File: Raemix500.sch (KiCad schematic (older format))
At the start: 0 parts

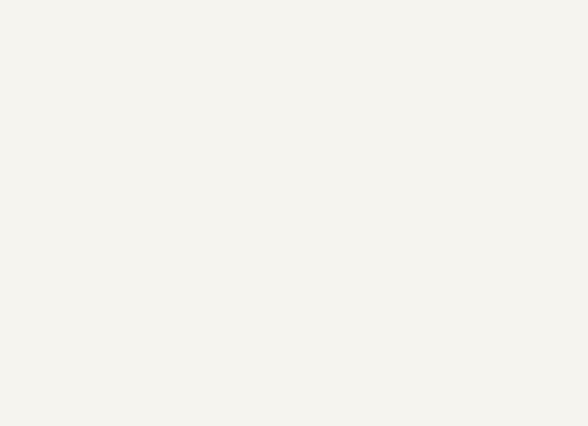
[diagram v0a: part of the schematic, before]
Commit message: Add expansion bus
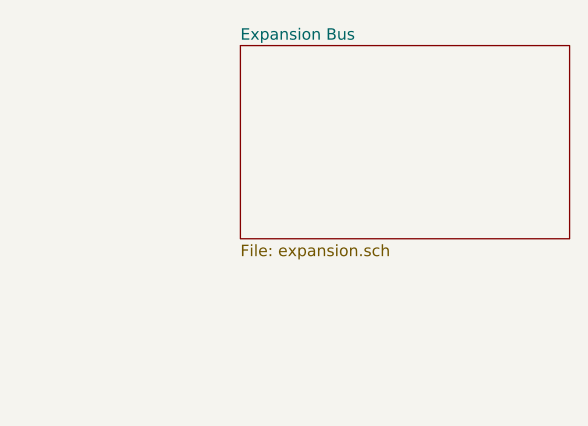
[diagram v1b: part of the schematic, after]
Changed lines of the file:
@@
 $Descr A4 11693 8268
 encoding utf-8
-Sheet 1 10
+Sheet 1 11
 Title "Rämixx500"
 Date "2019-04-17"
@@
 F1 "clockdist.sch" 50
 $EndSheet
+$Sheet
+S 9455 1420 1440 845
+U 5E813DC5
+F0 "Expansion Bus" 50
+F1 "expansion.sch" 50
+$EndSheet
 $EndSCHEMATC

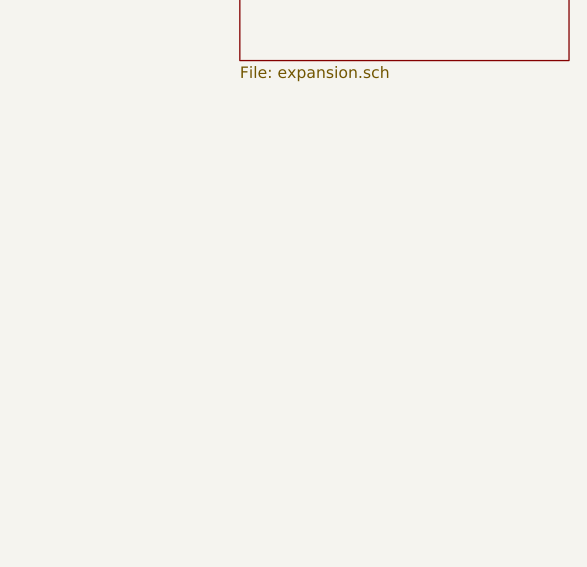
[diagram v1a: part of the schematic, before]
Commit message: Add power & decoupling, not yet complete
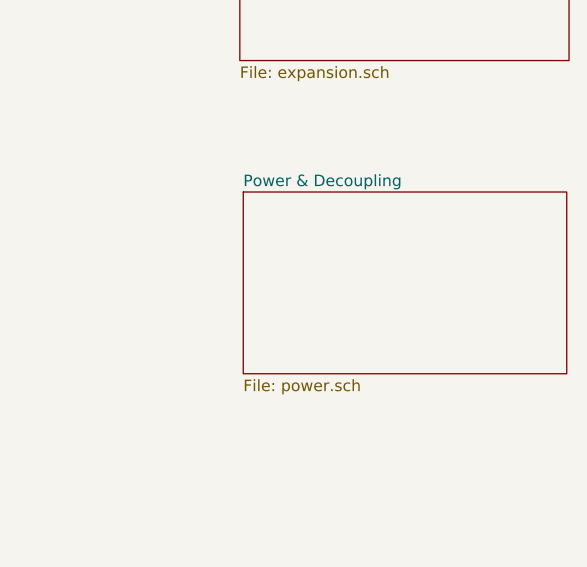
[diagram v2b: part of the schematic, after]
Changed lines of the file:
@@
 $Descr A4 11693 8268
 encoding utf-8
-Sheet 1 11
+Sheet 1 12
 Title "Rämixx500"
 Date "2019-04-17"
@@
 F1 "expansion.sch" 50
 $EndSheet
+$Sheet
+S 9470 2840 1415 795
+U 5E9E4C57
+F0 "Power & Decoupling" 50
+F1 "power.sch" 50
+$EndSheet
 $EndSCHEMATC

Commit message: Add RTC
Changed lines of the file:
@@
 $Descr A4 11693 8268
 encoding utf-8
-Sheet 1 12
+Sheet 1 13
 Title "Rämixx500"
 Date "2019-04-17"
@@
 F1 "power.sch" 50
 $EndSheet
+$Sheet
+S 4060 4220 1380 860
+U 5CF615AB
+F0 "Real-Time Clock" 50
+F1 "rtc.sch" 50
+$EndSheet
 $EndSCHEMATC

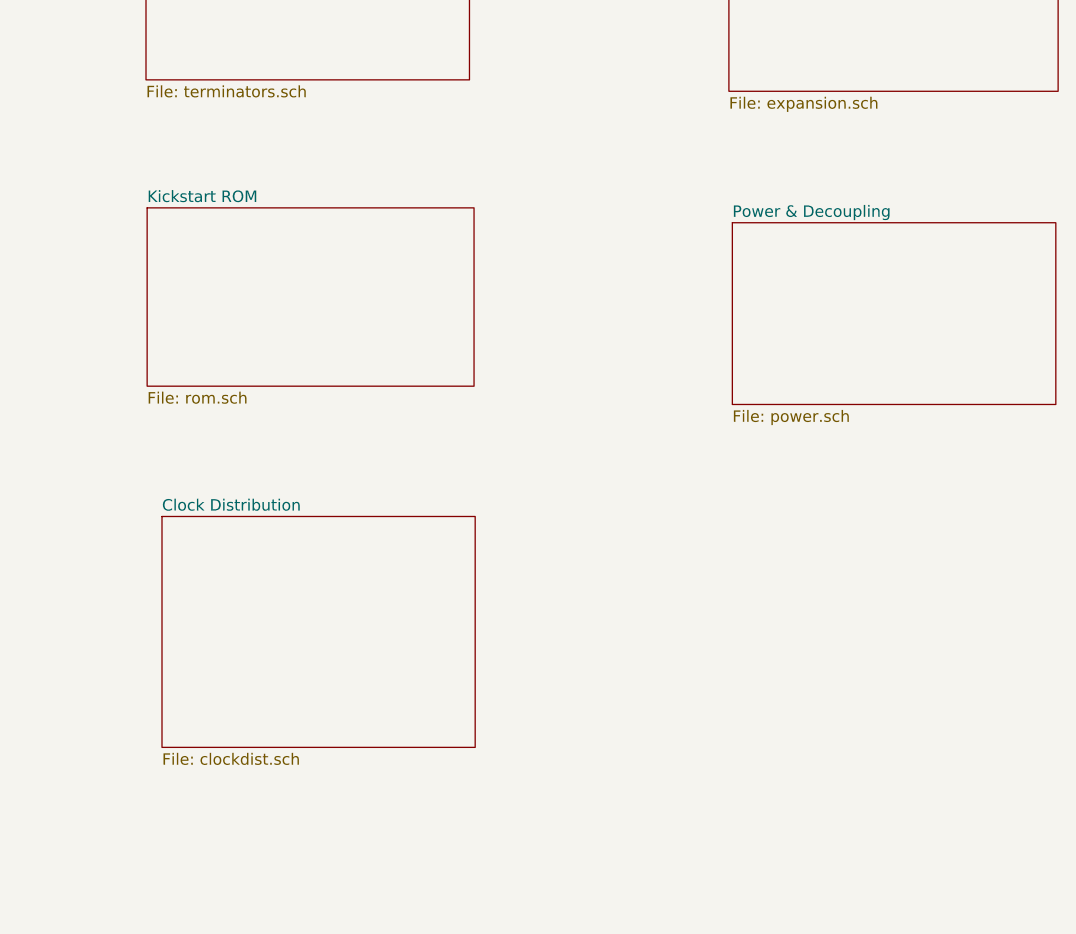
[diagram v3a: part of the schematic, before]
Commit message: Add trapdoor connector
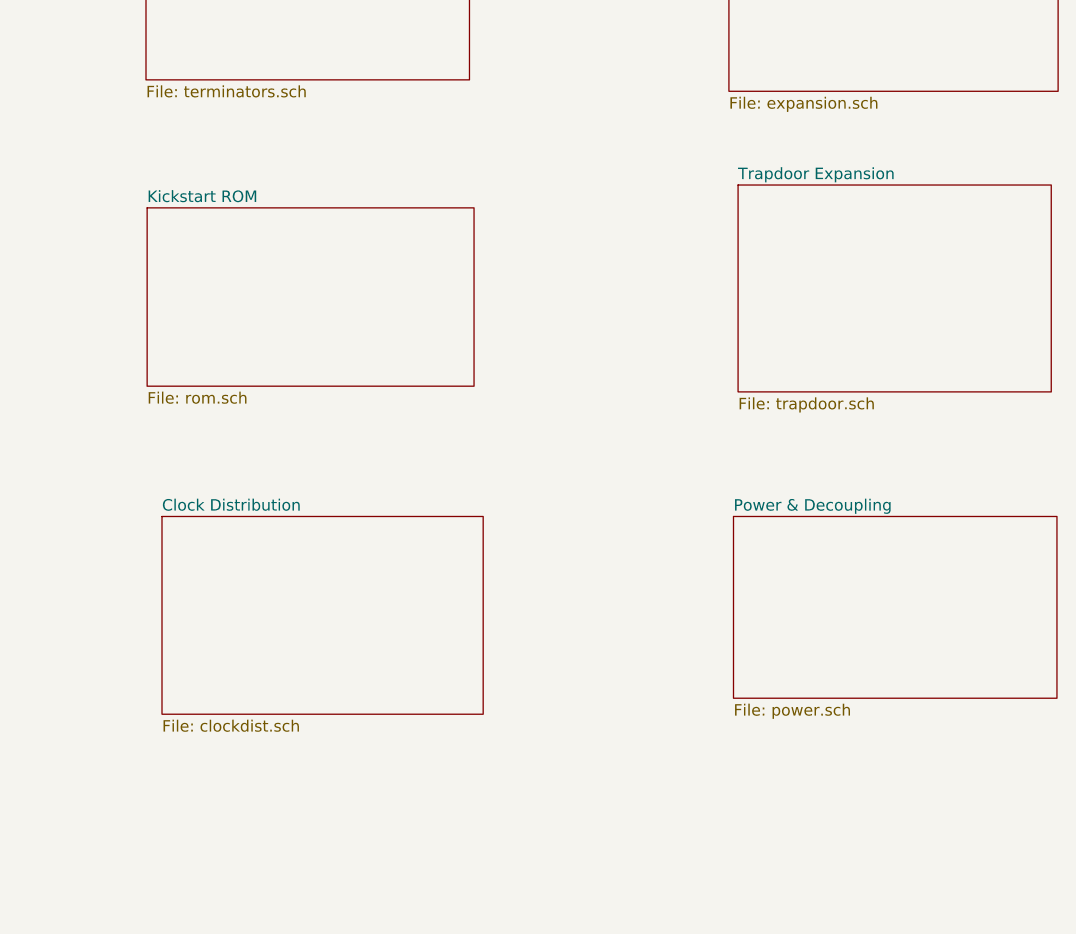
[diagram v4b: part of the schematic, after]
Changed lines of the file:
@@
 $Descr A4 11693 8268
 encoding utf-8
-Sheet 1 13
+Sheet 1 14
 Title "Rämixx500"
 Date "2019-04-17"
@@
 $EndSheet
 $Sheet
-S 6975 4125 1370 1010
+S 6975 4125 1405 865
 U 5D88EC26
 F0 "Clock Distribution" 50
@@
 $EndSheet
 $Sheet
-S 9470 2840 1415 795
+S 9475 4125 1415 795
 U 5E9E4C57
 F0 "Power & Decoupling" 50
@@
 F1 "rtc.sch" 50
 $EndSheet
+$Sheet
+S 9495 2675 1370 905
+U 5D00C589
+F0 "Trapdoor Expansion" 50
+F1 "trapdoor.sch" 50
+$EndSheet
 $EndSCHEMATC

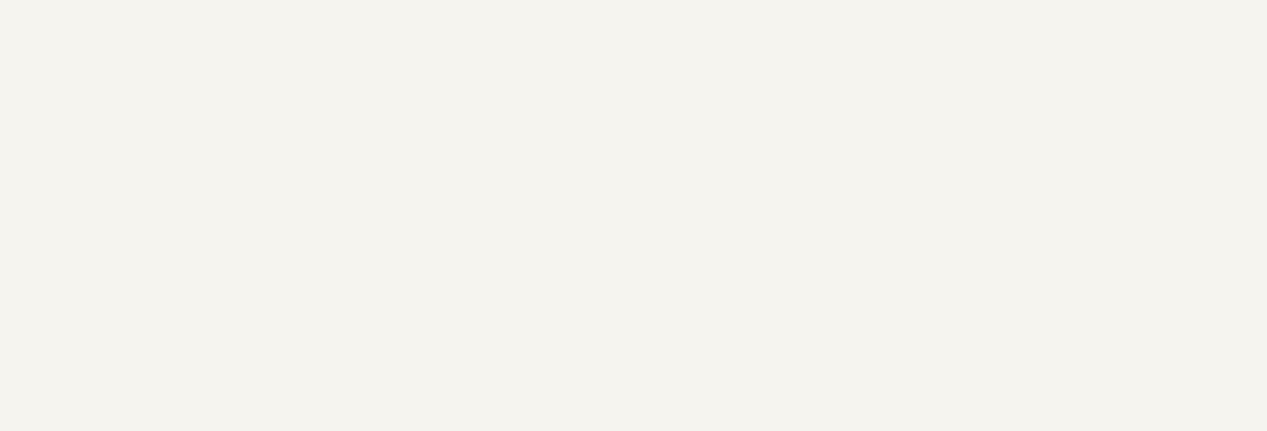
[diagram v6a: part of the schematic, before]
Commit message: Add OSHW & KiCad logos
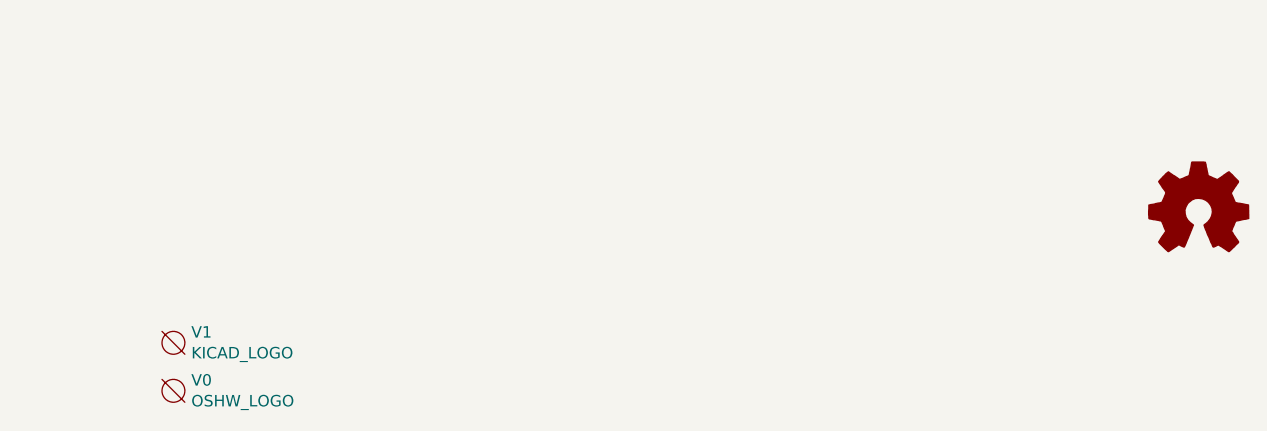
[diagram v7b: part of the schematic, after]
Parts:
- added V0: OSHW_LOGO, Symbol:OSHW-Logo2_14.6x12mm_Copper, symbol void:Void
- added V1: KICAD_LOGO, Symbol:KiCad-Logo2_12mm_SilkScreen, symbol void:Void
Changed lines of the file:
@@
 Sheet 1 14
 Title "Rämixx500"
-Date "2019-04-17"
+Date "2020-04-11"
 Rev "1git"
 Comp "SukkoPera"
@@
 F1 "trapdoor.sch" 50
 $EndSheet
+$Comp
+L Graphic:Logo_Open_Hardware_Small #LOGO1
+U 1 1 5ED3E3EE
+P 10865 6860
+F 0 "#LOGO1" H 10865 7135 50  0001 C CNN
+F 1 "Logo_Open_Hardware_Small" H 10865 6635 50  0001 C CNN
+F 2 "" H 10865 6860 50  0001 C CNN
+F 3 "~" H 10865 6860 50  0001 C CNN
+	1    10865 6860
+	1    0    0    -1
+$EndComp
+$Comp
+L void:Void V0
+U 1 1 5ED3E7FB
+P 6380 7640
+F 0 "V0" H 6458 7686 50  0000 L CNN
+F 1 "OSHW_LOGO" H 6458 7595 50  0000 L CNN
+F 2 "Symbol:OSHW-Logo2_14.6x12mm_Copper" H 6380 7640 50  0001 C CNN
+F 3 "" H 6380 7640 50  0001 C CNN
+	1    6380 7640
+	1    0    0    -1
+$EndComp
+$Comp
+L void:Void V1
+U 1 1 5ED79790
+P 6380 7430
+F 0 "V1" H 6458 7476 50  0000 L CNN
+F 1 "KICAD_LOGO" H 6458 7385 50  0000 L CNN
+F 2 "Symbol:KiCad-Logo2_12mm_SilkScreen" H 6380 7430 50  0001 C CNN
+F 3 "" H 6380 7430 50  0001 C CNN
+	1    6380 7430
+	1    0    0    -1
+$EndComp
 $EndSCHEMATC

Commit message: Add logos and credits
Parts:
- V0: footprint Symbol:OSHW-Logo2_14.6x12mm_Copper -> Symbol:OSHW-Logo2_14.6x12mm_SilkScreen
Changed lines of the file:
@@
 F 0 "V0" H 6458 7686 50  0000 L CNN
 F 1 "OSHW_LOGO" H 6458 7595 50  0000 L CNN
-F 2 "Symbol:OSHW-Logo2_14.6x12mm_Copper" H 6380 7640 50  0001 C CNN
+F 2 "Symbol:OSHW-Logo2_14.6x12mm_SilkScreen" H 6380 7640 50  0001 C CNN
 F 3 "" H 6380 7640 50  0001 C CNN
 	1    6380 7640
